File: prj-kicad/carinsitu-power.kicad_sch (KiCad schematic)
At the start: 9 parts, among them U6 TPS560200

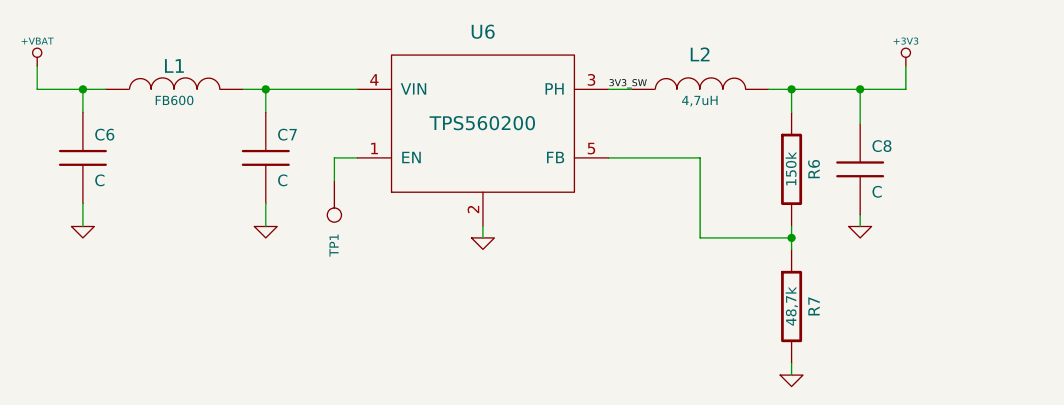
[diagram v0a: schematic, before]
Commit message: Fix schematic DRC
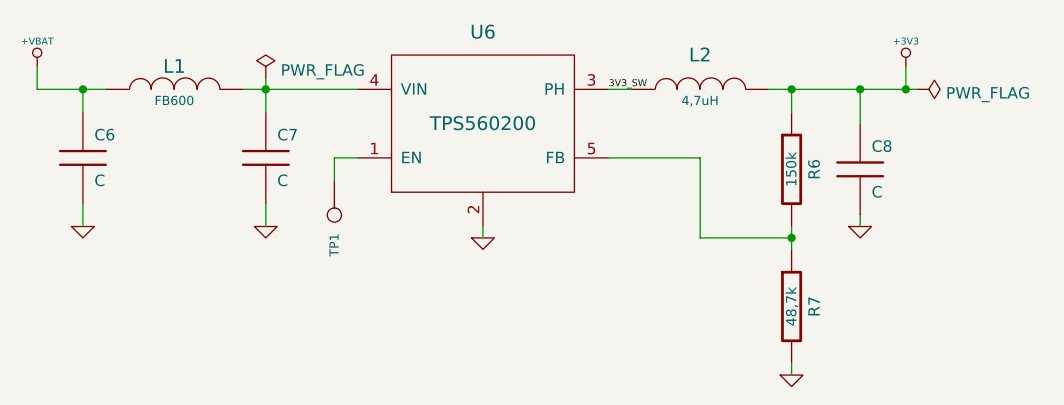
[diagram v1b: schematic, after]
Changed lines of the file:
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@@
   (junction (at 185.42 33.02) (diameter 0) (color 0 0 0 0)
   )
+  (junction (at 190.5 33.02) (diameter 0) (color 0 0 0 0)
+  )
   (junction (at 177.8 33.02) (diameter 0) (color 0 0 0 0)
   )
@@
     (stroke (width 0) (type default) (color 0 0 0 0))
   )
+  (wire (pts (xy 190.5 33.02) (xy 191.77 33.02))
+    (stroke (width 0) (type default) (color 0 0 0 0))
+  )
   (wire (pts (xy 119.38 33.02) (xy 129.54 33.02))
     (stroke (width 0) (type default) (color 0 0 0 0))
@@
   )
   (wire (pts (xy 93.98 33.02) (xy 99.06 33.02))
+    (stroke (width 0) (type default) (color 0 0 0 0))
+  )
+  (wire (pts (xy 119.38 31.75) (xy 119.38 33.02))
     (stroke (width 0) (type default) (color 0 0 0 0))
   )
@@
     (pin "1")
   )
-  (symbol (lib_id "carinsitu:INDUCTOR") (at 109.22 33.02 90) (unit 1)
+  (symbol (lib_name "INDUCTOR_1") (lib_id "carinsitu:INDUCTOR") (at 109.22 33.02 90) (unit 1)
     (in_bom yes) (on_board yes)
     (property "Reference" "L1" (id 0) (at 109.22 30.48 90)
@@
     )
     (pin "1")
+  )
+  (symbol (lib_id "power:PWR_FLAG") (at 191.77 33.02 270) (unit 1)
+    (in_bom yes) (on_board yes) (fields_autoplaced)
+    (property "Reference" "#FLG0102" (id 0) (at 193.675 33.02 0)
+      (effects (font (size 1.27 1.27)) hide)
+    )
+    (property "Value" "PWR_FLAG" (id 1) (at 194.945 33.4538 90)
+      (effects (font (size 1.27 1.27)) (justify left))
+    )
+    (property "Footprint" "" (id 2) (at 191.77 33.02 0)
+      (effects (font (size 1.27 1.27)) hide)
+    )
+    (property "Datasheet" "~" (id 3) (at 191.77 33.02 0)
+      (effects (font (size 1.27 1.27)) hide)
+    )
+    (pin "1")
+  )
+  (symbol (lib_id "power:PWR_FLAG") (at 119.38 31.75 0) (mirror y) (unit 1)
+    (in_bom yes) (on_board yes) (fields_autoplaced)
+    (property "Reference" "#FLG0103" (id 0) (at 119.38 29.845 0)
+      (effects (font (size 1.27 1.27)) hide)
+    )
+    (property "Value" "PWR_FLAG" (id 1) (at 121.031 30.9138 0)
+      (effects (font (size 1.27 1.27)) (justify right))
+    )
+    (property "Footprint" "" (id 2) (at 119.38 31.75 0)
+      (effects (font (size 1.27 1.27)) hide)
+    )
+    (property "Datasheet" "~" (id 3) (at 119.38 31.75 0)
+      (effects (font (size 1.27 1.27)) hide)
+    )
+    (pin "1")
